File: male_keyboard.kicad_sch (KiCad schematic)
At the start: 42 parts, among them J1 Elite-Pi Microcontroller, J2 AudioJack4, J3 AudioJack4, J4 Elite-Pi Microcontroller, SW1 SW_MEC_5G, SW10 SW_Push, SW11 SW_Push, SW12 SW_Push, SW13 SW_Push, SW14 SW_Push, SW15 SW_Push, SW16 SW_Push, SW17 SW_Push, SW18 SW_Push, SW19 SW_Push, SW2 SW_Push, SW20 SW_Push, SW21 SW_Push, SW22 SW_Push, SW23 SW_Push, SW24 SW_Push, SW25 SW_Push, SW26 SW_Push, SW27 SW_Push, SW28 SW_Push, SW29 SW_Push, SW3 SW_Push, SW30 SW_Push, SW31 SW_Push, SW32 SW_Push, SW33 SW_Push, SW34 SW_Push, SW35 SW_Push, SW36 SW_Push, SW37 SW_Push, SW38 SW_MEC_5G, SW4 SW_Push, SW5 SW_Push, SW6 SW_Push, SW7 SW_Push, SW8 SW_Push, SW9 SW_Push

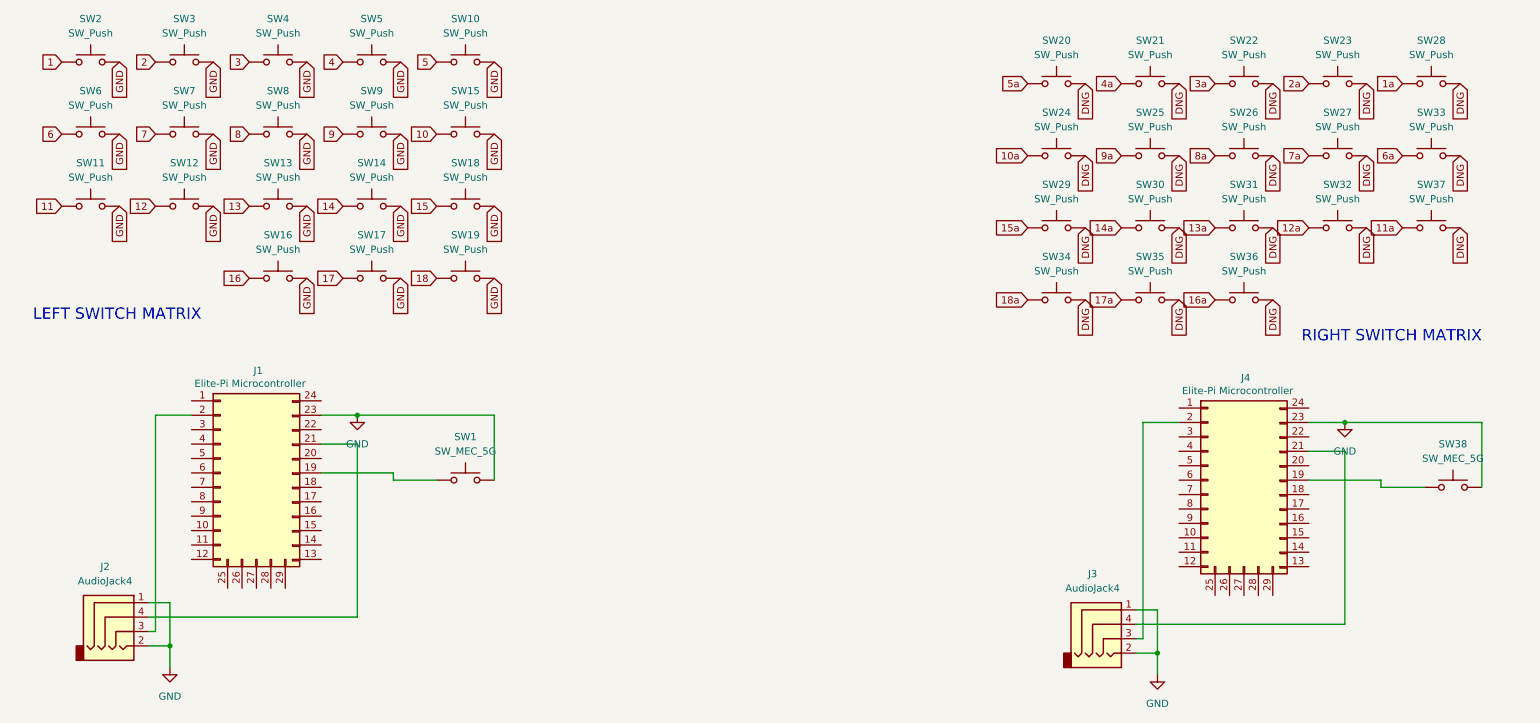
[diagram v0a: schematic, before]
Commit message: Label controller
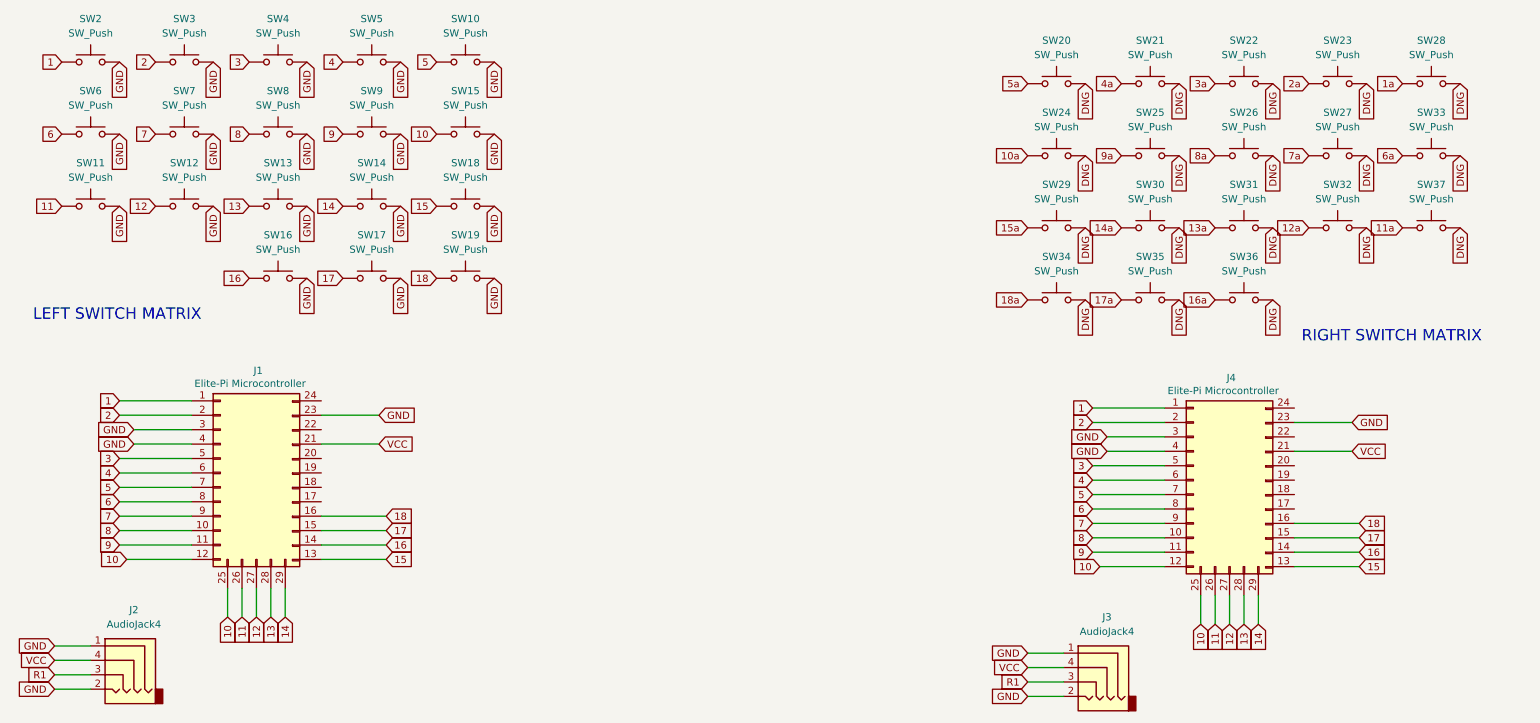
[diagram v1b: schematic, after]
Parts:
- removed SW1, SW38: SW_MEC_5G, Button_Switch_Keyboard:SW_Cherry_MX_1.00u_PCB, symbol Switch:SW_MEC_5G
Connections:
- net 1: now also J1.1 (Pin_1), J4.1 (Pin_1)
- net 10: now also J1.12 (Pin_12), J1.25 (Pin_25), J4.12 (Pin_12), J4.25 (Pin_25)
- net 11: now also J1.26 (Pin_26), J4.26 (Pin_26)
- net 12: now also J1.27 (Pin_27), J4.27 (Pin_27)
- net 13: now also J1.28 (Pin_28), J4.28 (Pin_28)
- net 14: now also J1.29 (Pin_29), J4.29 (Pin_29)
- net 15: now also J1.13 (Pin_13), J4.13 (Pin_13)
- net 16: now also J1.14 (Pin_14), J4.14 (Pin_14)
- net 17: now also J1.15 (Pin_15), J4.15 (Pin_15)
- net 18: now also J1.16 (Pin_16), J4.16 (Pin_16)
- net 2: now also J1.2 (Pin_2), J4.2 (Pin_2)
- net 3: now also J1.5 (Pin_5), J4.5 (Pin_5)
- net 4: now also J1.6 (Pin_6), J4.6 (Pin_6)
- net 5: now also J1.7 (Pin_7), J4.7 (Pin_7)
- net 6: now also J1.8 (Pin_8), J4.8 (Pin_8)
- net 7: now also J1.9 (Pin_9), J4.9 (Pin_9)
- net 8: now also J1.10 (Pin_10), J4.10 (Pin_10)
- net 9: now also J1.11 (Pin_11), J4.11 (Pin_11)
- net GND: now also J1.3 (Pin_3), J1.4 (Pin_4), J4.3 (Pin_3), J4.4 (Pin_4)
- net R1: now reaches J2.3
- net R1: now also J3.3; no longer J1.2 (Pin_2)
- net VCC: now reaches J1.21 (Pin_21), J2.4
- net VCC: now also J3.4, J4.21 (Pin_21)
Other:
- moved on the sheet: J2

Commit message: sort pcb
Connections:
- net 1: no longer J4.1 (Pin_1)
- net 10: no longer J4.12 (Pin_12), J4.25 (Pin_25)
- net 10a: now also J4.12 (Pin_12), J4.25 (Pin_25)
- net 11: no longer J4.26 (Pin_26)
- net 11a: now also J4.26 (Pin_26)
- net 12: no longer J4.27 (Pin_27)
- net 12a: now also J4.27 (Pin_27)
- net 13: no longer J4.28 (Pin_28)
- net 13a: now also J4.28 (Pin_28)
- net 14: no longer J4.29 (Pin_29)
- net 14a: now also J4.29 (Pin_29)
- net 15: no longer J4.13 (Pin_13)
- net 15a: now also J4.13 (Pin_13)
- net 16: no longer J4.14 (Pin_14)
- net 16a: now also J4.14 (Pin_14)
- net 17: no longer J4.15 (Pin_15)
- net 17a: now also J4.15 (Pin_15)
- net 18: no longer J4.16 (Pin_16)
- net 18a: now also J4.16 (Pin_16)
- net 1a: now also J4.1 (Pin_1)
- net 2: no longer J4.2 (Pin_2)
- net 2a: now also J4.2 (Pin_2)
- net 3: no longer J4.5 (Pin_5)
- net 3a: now also J4.5 (Pin_5)
- net 4: no longer J4.6 (Pin_6)
- net 4a: now also J4.6 (Pin_6)
- net 5: no longer J4.7 (Pin_7)
- net 6: no longer J4.8 (Pin_8)
- net 6a: now also J4.8 (Pin_8)
- net 7: no longer J4.9 (Pin_9)
- net 7a: now also J4.9 (Pin_9)
- net 8: no longer J4.10 (Pin_10)
- net 8a: now also J4.10 (Pin_10)
- net 9: no longer J4.11 (Pin_11)
- net 9a: now also J4.11 (Pin_11)
- net DNG: now also J3.1, J3.2, J4.23 (Pin_23), J4.3 (Pin_3), J4.4 (Pin_4)
- net GND: no longer J3.1, J3.2, J4.23 (Pin_23), J4.3 (Pin_3), J4.4 (Pin_4)
- net 5a renamed 20
- net 20: now also J4.7 (Pin_7)

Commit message: right side references
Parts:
- renumbered SW20 to SW19, SW21 to SW20, SW22 to SW21, SW23 to SW22, SW28 to SW23, SW33 to SW28, SW37 to SW33
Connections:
- net 20: now also J4.2 (Pin_2), SW20.1; no longer J4.7 (Pin_7), SW19.1
- removed net 10a: J4.12 (Pin_12), J4.25 (Pin_25), SW24.1
- net 11a renamed 30
- net 30: now also SW30.1; no longer SW33.1
- net 12a renamed 31
- net 31: now also SW31.1; no longer SW32.1
- net 13a renamed 32
- net 32: now also SW32.1; no longer SW31.1
- net 14a renamed 33
- net 33: now also SW33.1; no longer SW30.1
- net 15a renamed 29
- net 29: now also J4.25 (Pin_25); no longer J4.13 (Pin_13)
- net 16a renamed 35
- net 35: now also SW35.1; no longer SW36.1
- net 17a renamed 36
- net 36: now also SW36.1; no longer SW35.1
- net 18a: no longer names the net of J4.16 (Pin_16)
- net 18a: no longer SW34.1
- net 1a renamed 19
- net 19: now also SW19.1; no longer SW23.1
- net 2a renamed 22
- net 22: now also J4.6 (Pin_6); no longer J4.2 (Pin_2)
- net 3a renamed 21
- removed net 4a: J4.6 (Pin_6), SW20.1
- net 6a renamed 24
- net 24: now also SW24.1; no longer SW28.1
- net 7a renamed 25
- net 25: now also SW25.1; no longer SW27.1
- net 8a renamed 26
- net 9a renamed 27
- net 27: now also SW27.1; no longer SW25.1
- new net 23: J4.7 (Pin_7), SW23.1
- new net 28: J4.12 (Pin_12), SW28.1
- new net 34: J4.13 (Pin_13), SW34.1
